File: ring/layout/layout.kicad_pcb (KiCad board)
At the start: 2 copper layers, 62 x 6.2 mm, 62 parts, among them U1 ?, U10 ?, U11 ?, U12 ?, U13 ?, U14 ?, U15 ?, U2 ?, U3 ?, U4 ?, U5 ?, U6 ?, U7 ?, U8 ?, U9 ?, Y1 38.4MHz

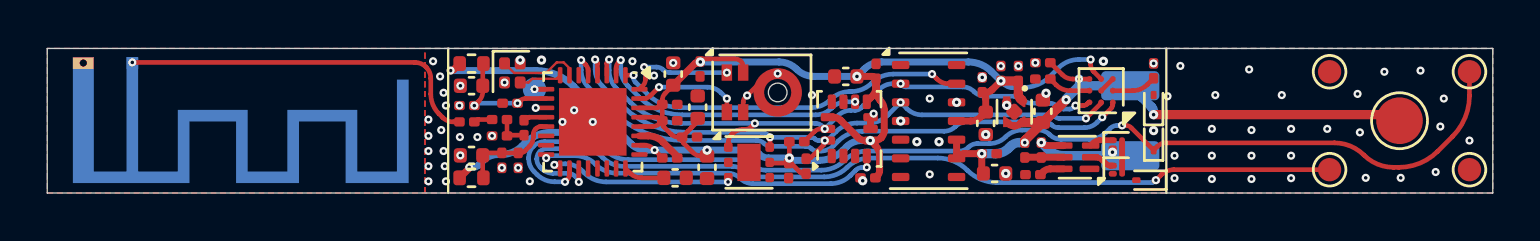
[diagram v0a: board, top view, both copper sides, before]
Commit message: moved antenna and drc fully passes
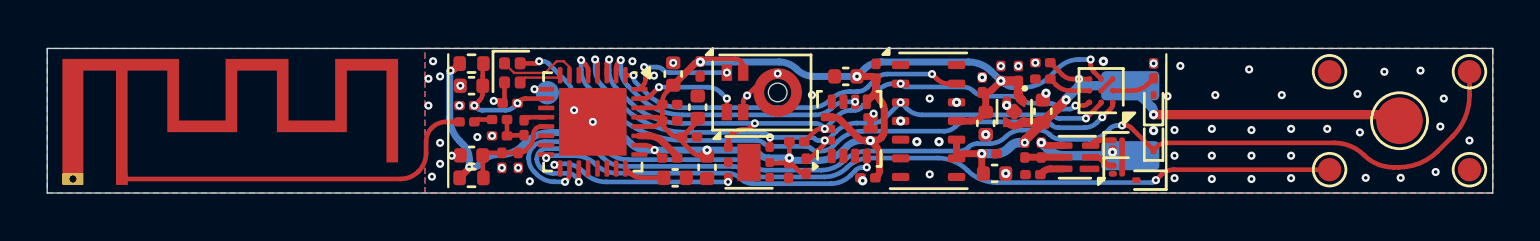
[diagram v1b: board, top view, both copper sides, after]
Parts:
- U7: moved to F.Cu
- moved U7 5.00 mm to (123.0, 85.6)
- moved TP1 0.57 mm to (141.2, 81.9)
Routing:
- net GND: track 6.02 -> 11.4 mm, vias 82 -> 72
- net VDD: track 77.8 -> 74.2 mm
- net rst: track 0.50 -> 1.10 mm
- net cpu.ant.out3: track 15.8 -> 16.1 mm, vias 1 -> 0
